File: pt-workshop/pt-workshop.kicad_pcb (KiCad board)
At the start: 4 copper layers, 22.9 x 68.6 mm, 88 parts, among them J103 Conn_01x20, J104 Conn_01x20, Q301 NST65011, U201 L78L05, U202 PT2399-Detailed, U301 TL972

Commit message: wip
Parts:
- removed kibuzzard-65ABC4A4: G***, kibuzzard-65ABC4A4
- added kibuzzard-65E1A759: G***, kibuzzard-65E1A759, F.Cu at (36.8, 52.4)
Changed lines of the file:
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@@
       (net 2 "/PT_GND") (pinfunction "1") (pintype "input"))
   )
+  (footprint "kibuzzard-65E1A759" (layer "F.Cu")
+    (at 36.83 52.4)
+    (descr "Generated with KiBuzzard")
+    (tags "kb_params=eyJBbGlnbm1lbnRDaG9pY2UiOiAiQ2VudGVyIiwgIkNhcExlZnRDaG9pY2UiOiAiIiwgIkNhcFJpZ2h0Q2hvaWNlIjogIiIsICJGb250Q29tYm9Cb3giOiAiTW9uSHVnby1vdXQiLCAiSGVpZ2h0Q3RybCI6ICIzIiwgIkxheWVyQ29tYm9Cb3giOiAiRi5TaWxrUyIsICJNdWx0aUxpbmVUZXh0IjogIlBUVCIsICJQYWRkaW5nQm90dG9tQ3RybCI6ICI1IiwgIlBhZGRpbmdMZWZ0Q3RybCI6ICI1IiwgIlBhZGRpbmdSaWdodEN0cmwiOiAiNSIsICJQYWRkaW5nVG9wQ3RybCI6ICI1IiwgIldpZHRoQ3RybCI6ICIzIn0=")
+    (attr board_only exclude_from_pos_files exclude_from_bom)
+    (fp_text reference "kibuzzard-65E1A759" (at 0 -5.42925) (layer "F.SilkS") hide
+      (effects (font (size 0 0)))
+    )
+    (fp_text value "G***" (at 0 5.42925) (layer "F.SilkS") hide
+      (effects (font (size 0 0)))
+    )
+    (fp_poly (pts
+        (xy 0.904875 2.38125)
+        (xy 0.904875 -2.38125)
+        (xy 2.714625 -2.38125)
+        (xy 2.714625 2.38125)
+        (xy 1.190625 2.38125)
+        (xy 1.190625 1.190625)
+        (xy 2.428875 1.190625)
+        (xy 2.428875 0.904875)
+        (xy 1.952625 0.904875)
+        (xy 1.952625 -0.904875)
+        (xy 2.428875 -0.904875)
+        (xy 2.428875 -1.190625)
+        (xy 1.952625 -1.190625)
+        (xy 1.952625 -1.61925)
+        (xy 1.190625 -1.61925)
+        (xy 1.190625 1.190625)
+        (xy 1.190625 2.38125)
+        (xy 0.904875 2.38125)
+      ) (layer "F.SilkS") (width 0) (fill solid))
+    (fp_poly (pts
+        (xy -2.714625 2.38125)
+        (xy -2.714625 -2.38125)
+        (xy -0.333375 -2.38125)
+        (xy -0.333375 2.38125)
+        (xy -2.428875 2.38125)
+        (xy -2.428875 1.905)
+        (xy -1.666875 1.905)
+        (xy -1.666875 1.190625)
+        (xy -0.619125 1.190625)
+        (xy -0.619125 -1.190625)
+        (xy -2.428875 -1.190625)
+        (xy -2.428875 1.905)
+        (xy -2.428875 2.38125)
+        (xy -2.714625 2.38125)
+      ) (layer "F.SilkS") (width 0) (fill solid))
+    (fp_poly (pts
+        (xy -0.619125 2.38125)
+        (xy -0.619125 -2.38125)
+        (xy 1.190625 -2.38125)
+        (xy 1.190625 2.38125)
+        (xy -0.333375 2.38125)
+        (xy -0.333375 1.190625)
+        (xy 0.904875 1.190625)
+        (xy 0.904875 0.904875)
+        (xy 0.428625 0.904875)
+        (xy 0.428625 -0.904875)
+        (xy 0.904875 -0.904875)
+        (xy 0.904875 -1.190625)
+        (xy 0.428625 -1.190625)
+        (xy 0.428625 -1.61925)
+        (xy -0.333375 -1.61925)
+        (xy -0.333375 1.190625)
+        (xy -0.333375 2.38125)
+        (xy -0.619125 2.38125)
+      ) (layer "F.SilkS") (width 0) (fill solid))
+    (fp_poly (pts
+        (xy -2.143125 0.142875)
+        (xy -2.143125 -0.142875)
+        (xy -0.904875 -0.142875)
+        (xy -0.904875 0.142875)
+        (xy -2.143125 0.142875)
+      ) (layer "F.SilkS") (width 0) (fill solid))
+  )
   (footprint "Resistor_SMD:R_0603_1608Metric_Pad0.98x0.95mm_HandSolder" (layer "F.Cu")
     (at 42.672 97.212 90)
@@
     )
   )
-  (footprint "kibuzzard-65ABC4A4" (layer "F.Cu")
-    (at 36.83 53.34)
-    (descr "Generated with KiBuzzard")
-    (tags "kb_params=eyJBbGlnbm1lbnRDaG9pY2UiOiAiQ2VudGVyIiwgIkNhcExlZnRDaG9pY2UiOiAiPiIsICJDYXBSaWdodENob2ljZSI6ICI8IiwgIkZvbnRDb21ib0JveCI6ICJNb2RlcmF0LU1vbm8tTWVkaXVtIiwgIkhlaWdodEN0cmwiOiAiMSIsICJMYXllckNvbWJvQm94IjogIkYuU2lsa1MiLCAiTXVsdGlMaW5lVGV4dCI6ICJQVFQiLCAiUGFkZGluZ0JvdHRvbUN0cmwiOiAiNSIsICJQYWRkaW5nTGVmdEN0cmwiOiAiNSIsICJQYWRkaW5nUmlnaHRDdHJsIjogIjUiLCAiUGFkZGluZ1RvcEN0cmwiOiAiNSIsICJXaWR0aEN0cmwiOiAiNy40In0=")
-    (attr board_only exclude_from_pos_files exclude_from_bom)
-    (fp_text reference "kibuzzard-65ABC4A4" (at 0 -3.934354) (layer "F.SilkS") hide
-      (effects (font (size 0 0) (thickness 0.15)))
-    )
-    (fp_text value "G***" (at 0 3.934354) (layer "F.SilkS") hide
-      (effects (font (size 0 0) (thickness 0.15)))
-    )
-    (fp_poly (pts
-        (xy -0.9652 -0.01905)
-        (xy -0.875308 -0.032147)
-        (xy -0.808831 -0.071438)
-        (xy -0.767755 -0.133747)
-        (xy -0.754063 -0.2159)
-        (xy -0.767755 -0.295473)
-        (xy -0.808831 -0.356394)
-        (xy -0.872927 -0.395089)
-        (xy -0.955675 -0.407987)
-        (xy -1.173163 -0.407987)
-        (xy -1.173163 -0.01905)
-        (xy -0.9652 -0.01905)
-      ) (layer "F.SilkS") (width 0) (fill solid))
-    (fp_poly (pts
-        (xy -3.367898 -0.886354)
-        (xy -3.698627 -0.886354)
-        (xy -4.28953 -0.886354)
-        (xy -3.698627 0)
-        (xy -4.28953 0.886354)
-        (xy -3.698627 0.886354)
-        (xy -3.367898 0.886354)
-        (xy -1.173163 0.886354)
-        (xy -1.173163 0.555625)
-        (xy -1.335088 0.555625)
-        (xy -1.335088 -0.555625)
-        (xy -0.9271 -0.555625)
-        (xy -0.829381 -0.545218)
-        (xy -0.745772 -0.513997)
-        (xy -0.676275 -0.461963)
-        (xy -0.62424 -0.392994)
-        (xy -0.593019 -0.310974)
-        (xy -0.582613 -0.2159)
-        (xy -0.593196 -0.118181)
-        (xy -0.624946 -0.034572)
-        (xy -0.677863 0.034925)
-        (xy -0.748947 0.08696)
-        (xy -0.835201 0.118181)
-        (xy -0.936625 0.128588)
-        (xy -1.173163 0.128588)
-        (xy -1.173163 0.555625)
-        (xy -1.173163 0.886354)
-        (xy 0.065087 0.886354)
-        (xy 0.065087 0.555625)
-        (xy -0.1016 0.555625)
-        (xy -0.1016 -0.404812)
-        (xy -0.417513 -0.404812)
-        (xy -0.417513 -0.555625)
-        (xy 0.382587 -0.555625)
-        (xy 0.382587 -0.404812)
-        (xy 0.065087 -0.404812)
-        (xy 0.065087 0.555625)
-        (xy 0.065087 0.886354)
-        (xy 1.017588 0.886354)
-        (xy 1.017588 0.555625)
-        (xy 0.8509 0.555625)
-        (xy 0.8509 -0.404812)
-        (xy 0.534987 -0.404812)
-        (xy 0.534987 -0.555625)
-        (xy 1.335087 -0.555625)
-        (xy 1.335087 -0.404812)
-        (xy 1.017588 -0.404812)
-        (xy 1.017588 0.555625)
-        (xy 1.017588 0.886354)
-        (xy 3.367898 0.886354)
-        (xy 3.698627 0.886354)
-        (xy 4.28953 0.886354)
-        (xy 3.698627 0)
-        (xy 4.28953 -0.886354)
-        (xy 3.698627 -0.886354)
-        (xy 3.367898 -0.886354)
-        (xy -3.367898 -0.886354)
-      ) (layer "F.SilkS") (width 0) (fill solid))
-  )
   (footprint "Capacitor_SMD:C_0603_1608Metric_Pad1.08x0.95mm_HandSolder" (layer "F.Cu")

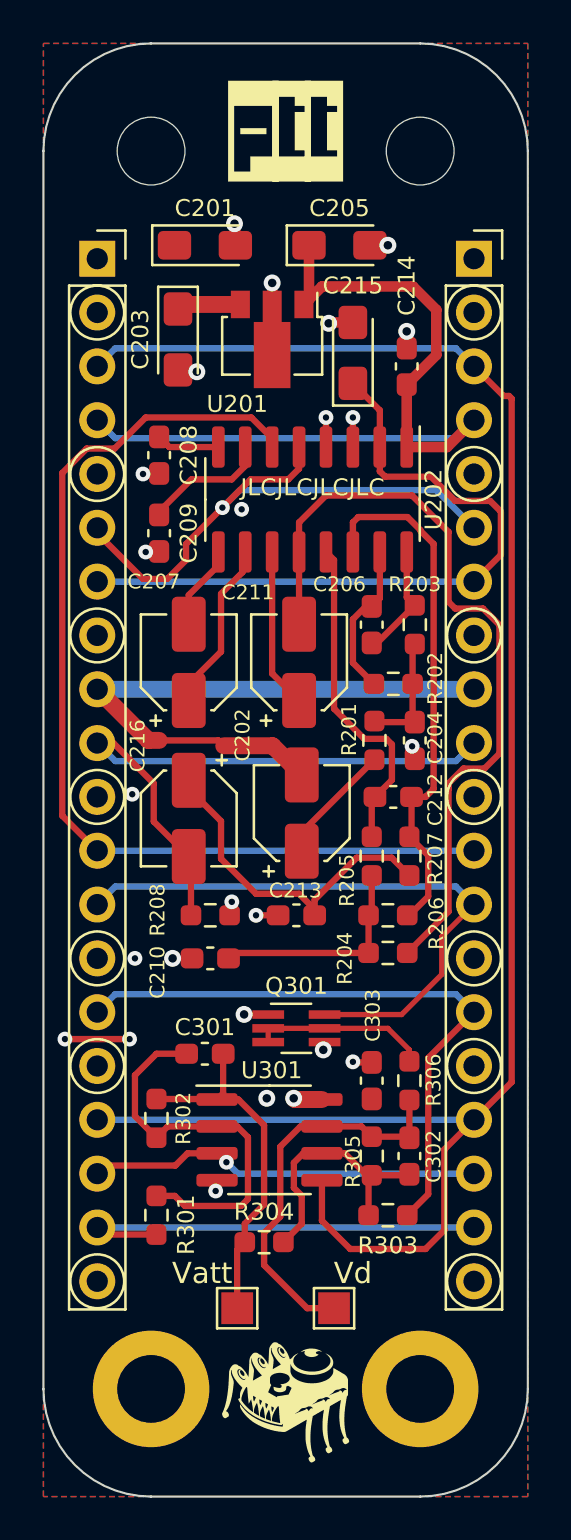
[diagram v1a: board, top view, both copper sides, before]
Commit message: PTT without attverts
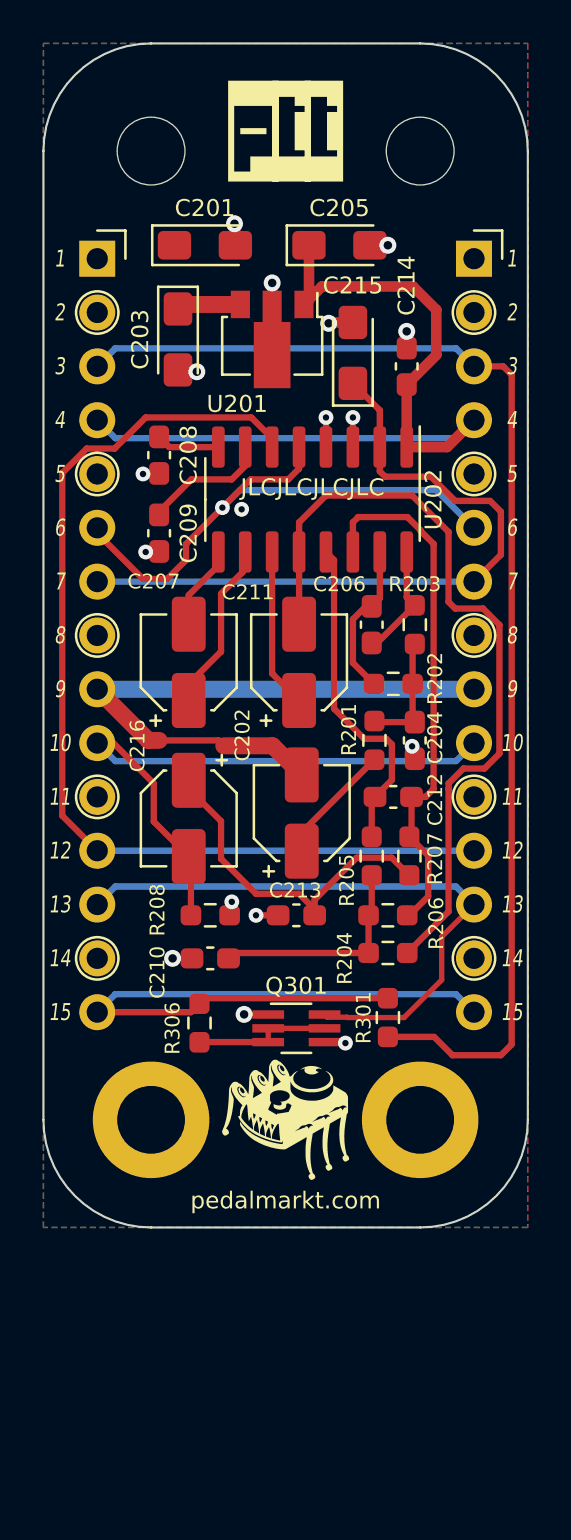
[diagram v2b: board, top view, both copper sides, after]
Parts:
- removed C301, C302: 10p, Capacitor_SMD:C_0603_1608Metric_Pad1.08x0.95mm_HandSolder
- removed C303: 100n, Capacitor_SMD:C_0603_1608Metric_Pad1.08x0.95mm_HandSolder
- removed R302, R303, R304, R305: 100K, Resistor_SMD:R_0603_1608Metric_Pad0.98x0.95mm_HandSolder
- removed TP1: Vatt, TestPoint:TestPoint_Pad_1.5x1.5mm
- removed TP2: Vd, TestPoint:TestPoint_Pad_1.5x1.5mm
- removed U301: TL972, Package_SO:SOIC-8_3.9x4.9mm_P1.27mm
- removed the kibuzzard-65AA5850 at (41.9, 96.5)
- removed the kibuzzard-65AA5850 at (41.9, 106.7)
- removed kibuzzard-65AA59F3: G***, kibuzzard-65AA59F3
- removed kibuzzard-65AA5C27: G***, kibuzzard-65AA5C27
- removed kibuzzard-65AA5C3F: G***, kibuzzard-65AA5C3F
- removed kibuzzard-65AA5C71: G***, kibuzzard-65AA5C71
- removed the kibuzzard-65AAA44C at (31.8, 96.5)
- removed the kibuzzard-65AAA44C at (31.8, 106.7)
- removed kibuzzard-65AAA4B9: G***, kibuzzard-65AAA4B9
- removed kibuzzard-65AAA4E9: G***, kibuzzard-65AAA4E9
- removed kibuzzard-65AAA4EF: G***, kibuzzard-65AAA4EF
- removed kibuzzard-65AAA518: G***, kibuzzard-65AAA518
- added kibuzzard-65FAB27A: G***, kibuzzard-65FAB27A, B.Cu at (31.8, 94.0)
- added kibuzzard-65FAB286: G***, kibuzzard-65FAB286, B.Cu at (41.9, 94.0)
- J103, J104: value Conn_01x20 -> Conn_01x15; footprint Connector_PinSocket_2.54mm:PinSocket_1x20_P2.54mm_Vertical -> Connector_PinSocket_2.54mm:PinSocket_1x15_P2.54mm_Vertical
- moved R301 14.4 mm to (41.7, 94.2)
- moved G*** 13.3 mm to (36.8, 99.1)
- moved H101 12.7 mm to (43.2, 99.1)
- moved H103 12.7 mm to (30.5, 99.1)
- moved R306 10.3 mm to (32.8, 94.5), turned to -90 degrees
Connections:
- J103 pad 15: /PT_Voffset -> /PT_Vctrl
- J104 pad 15: /PT_Voffset -> /PT_Vctrl
- R301 pad 1: /PT_AttVert3 -> /PT_4.5V
- R301 pad 2: Net-(C301-Pad1) -> /PT_Vctrl
- R306 pad 1: Net-(C302-Pad2) -> /PT_Vctrl
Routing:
- net /PT_Vctrl: track 0.00 -> 32.5 mm
- net /PT_4.5V: track 87.8 -> 58.4 mm
- net /PT_Voffset: track 29.4 -> 0.00 mm
- net /PT_AttVert3: track 20.7 -> 0.00 mm
- net Net-(C301-Pad1): track 18.5 -> 0.00 mm
- net Net-(C302-Pad2): track 18.5 -> 0.00 mm
- net /PT_AttVert2: track 18.0 -> 0.00 mm, vias 1 -> 0
- net Net-(C301-Pad2): track 17.0 -> 0.00 mm
- net Net-(C302-Pad1): track 12.3 -> 0.00 mm
- net /PT_9V: track 7.44 -> 3.03 mm, vias 5 -> 0
- net Net-(Q301-Pad2): track 8.28 -> 6.56 mm
- net /PT_GND: track 16.3 -> 15.5 mm, vias 20 -> 17
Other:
- board size 22.9 x 68.6 mm -> 22.9 x 55.9 mm
- board text added: "1"
- board text added: "10"
- board text added: "11"
- board text added: "12"
- board text added: "13"
- board text added: "14"
- board text added: "15"
- board text added: "2"
- board text added: "3"
- board text added: "4"
- board text added: "5"
- board text added: "6"
- board text added: "7"
- board text added: "8"
- board text added: "9"

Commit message: LFO graphics
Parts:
- removed kibuzzard-65AA5840: G***, kibuzzard-65AA5840
- removed kibuzzard-65AA5873: G***, kibuzzard-65AA5873
- removed kibuzzard-65AA58DD: G***, kibuzzard-65AA58DD
- removed kibuzzard-65AAA38B: G***, kibuzzard-65AAA38B
- removed kibuzzard-65AAA43F: G***, kibuzzard-65AAA43F
- removed kibuzzard-65AAA461: G***, kibuzzard-65AAA461
- removed kibuzzard-65FAB27A: G***, kibuzzard-65FAB27A
- removed kibuzzard-65FAB286: G***, kibuzzard-65FAB286
- added kibuzzard-65FC58C1: G***, kibuzzard-65FC58C1, B.Cu at (31.8, 58.4)
- added kibuzzard-65FC58C8: G***, kibuzzard-65FC58C8, B.Cu at (41.9, 58.4)
- added kibuzzard-65FC58D1: G***, kibuzzard-65FC58D1, B.Cu at (31.8, 63.5)
- added kibuzzard-65FC58D6: G***, kibuzzard-65FC58D6, B.Cu at (41.9, 63.5)
- added kibuzzard-65FC58DD: G***, kibuzzard-65FC58DD, B.Cu at (41.9, 66.0)
- added kibuzzard-65FC58E2: G***, kibuzzard-65FC58E2, B.Cu at (31.8, 66.0)
- added kibuzzard-65FC5A5D: G***, kibuzzard-65FC5A5D, B.Cu at (31.8, 94.0)
- added kibuzzard-65FC5A62: G***, kibuzzard-65FC5A62, B.Cu at (41.9, 94.0)
- G***: moved to B.Cu
- moved kibuzzard-65E1A759 46.7 mm to (36.8, 99.1)
- turned G*** to 180 degrees
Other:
- board text added: "v1rev1"
- board text removed: "PTT v1rev1"

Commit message: wip
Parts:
- removed REF**: OSHW-Logo2_7.3x6mm_SilkScreen, Symbol:OSHW-Logo2_7.3x6mm_SilkScreen
- removed kibuzzard-65AA5850 (x5): G***, kibuzzard-65AA5850
- removed kibuzzard-65AA58EE: G***, kibuzzard-65AA58EE
- removed kibuzzard-65AA5905: G***, kibuzzard-65AA5905
- removed kibuzzard-65AA592D: G***, kibuzzard-65AA592D
- removed kibuzzard-65AA59BE: G***, kibuzzard-65AA59BE
- removed kibuzzard-65AA5A57: G***, kibuzzard-65AA5A57
- removed kibuzzard-65AA5AB7: G***, kibuzzard-65AA5AB7
- removed kibuzzard-65AAA3AC: G***, kibuzzard-65AAA3AC
- removed kibuzzard-65AAA3BE: G***, kibuzzard-65AAA3BE
- removed kibuzzard-65AAA3D1: G***, kibuzzard-65AAA3D1
- removed kibuzzard-65AAA3DF: G***, kibuzzard-65AAA3DF
- removed kibuzzard-65AAA44C (x5): G***, kibuzzard-65AAA44C
- removed kibuzzard-65AAA47E: G***, kibuzzard-65AAA47E
- removed kibuzzard-65AAA49E: G***, kibuzzard-65AAA49E
- removed kibuzzard-65FC58C1: G***, kibuzzard-65FC58C1
- removed kibuzzard-65FC58C8: G***, kibuzzard-65FC58C8
- removed kibuzzard-65FC58D1: G***, kibuzzard-65FC58D1
- removed kibuzzard-65FC58D6: G***, kibuzzard-65FC58D6
- removed kibuzzard-65FC58DD: G***, kibuzzard-65FC58DD
- removed kibuzzard-65FC58E2: G***, kibuzzard-65FC58E2
- removed kibuzzard-65FC5A5D: G***, kibuzzard-65FC5A5D
- removed kibuzzard-65FC5A62: G***, kibuzzard-65FC5A62
- added kibuzzard-68A2FE01: G***, kibuzzard-68A2FE01, B.Cu at (31.8, 58.4)
- added kibuzzard-68A2FE06: G***, kibuzzard-68A2FE06, B.Cu at (31.8, 61.0)
- added kibuzzard-68A2FE0E: G***, kibuzzard-68A2FE0E, B.Cu at (31.8, 63.5)
- added kibuzzard-68A2FE18: G***, kibuzzard-68A2FE18, B.Cu at (31.5, 66.0)
- added kibuzzard-68A2FE1E: G***, kibuzzard-68A2FE1E, B.Cu at (31.8, 68.6)
- added kibuzzard-68A2FE25: G***, kibuzzard-68A2FE25, B.Cu at (31.5, 71.1)
- added kibuzzard-68A2FE2B: G***, kibuzzard-68A2FE2B, B.Cu at (31.5, 73.7)
- added kibuzzard-68A2FE30: G***, kibuzzard-68A2FE30, B.Cu at (31.8, 76.2)
- added kibuzzard-68A2FE36: G***, kibuzzard-68A2FE36, B.Cu at (31.8, 78.7)
- added kibuzzard-68A2FE3C: G***, kibuzzard-68A2FE3C, B.Cu at (32.3, 81.3)
- added kibuzzard-68A2FE41: G***, kibuzzard-68A2FE41, B.Cu at (31.5, 83.8)
- added kibuzzard-68A2FE46: G***, kibuzzard-68A2FE46, B.Cu at (32.3, 86.4)
- added kibuzzard-68A2FE4A: G***, kibuzzard-68A2FE4A, B.Cu at (32.8, 88.9)
- added kibuzzard-68A2FE4F: G***, kibuzzard-68A2FE4F, B.Cu at (31.8, 91.4)
- added kibuzzard-68A2FE55: G***, kibuzzard-68A2FE55, B.Cu at (32.3, 94.0)
- added kibuzzard-68A2FE5C: G***, kibuzzard-68A2FE5C, B.Cu at (41.9, 58.4)
- added kibuzzard-68A2FE62: G***, kibuzzard-68A2FE62, B.Cu at (41.9, 61.0)
- added kibuzzard-68A2FE67: G***, kibuzzard-68A2FE67, B.Cu at (41.9, 63.5)
- added kibuzzard-68A2FE6B: G***, kibuzzard-68A2FE6B, B.Cu at (41.9, 66.0)
- added kibuzzard-68A2FE71: G***, kibuzzard-68A2FE71, B.Cu at (41.9, 68.6)
- added kibuzzard-68A2FE76: G***, kibuzzard-68A2FE76, B.Cu at (41.9, 78.7)
- added kibuzzard-68A2FE7B: G***, kibuzzard-68A2FE7B, B.Cu at (41.9, 83.8)
- added kibuzzard-68A2FE80: G***, kibuzzard-68A2FE80, B.Cu at (41.4, 86.4)
- added kibuzzard-68A2FE85: G***, kibuzzard-68A2FE85, B.Cu at (40.9, 88.9)
- added kibuzzard-68A2FE8A: G***, kibuzzard-68A2FE8A, B.Cu at (41.9, 91.4)
- added kibuzzard-68A2FE8F: G***, kibuzzard-68A2FE8F, B.Cu at (41.4, 94.0)
- added kibuzzard-68A2FF07: G***, kibuzzard-68A2FF07, B.Cu at (41.4, 81.3)
- added kibuzzard-68A2FF19: G***, kibuzzard-68A2FF19, B.Cu at (41.9, 71.1)
- added kibuzzard-68A2FF1E: G***, kibuzzard-68A2FF1E, B.Cu at (41.9, 73.7)
- added kibuzzard-68A2FF23: G***, kibuzzard-68A2FF23, B.Cu at (41.9, 76.2)
- C208, C209, C214: value 100n -> 1u
- Q301: value NST65011 -> MMDT3904
- R207: value 5.6K -> 1k
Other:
- board text added: "v1rev3"
- board text removed: "v1rev1"
